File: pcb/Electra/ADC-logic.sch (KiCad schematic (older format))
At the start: 6 parts, among them J701 Conn_01x02_Female, J702 Conn_01x02_Female

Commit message: PCB Ver 1 completed (TODO: Check)
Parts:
- J701, J702: Package Reference - -> 2.54mm 1x2
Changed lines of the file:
@@
 $Descr A4 11693 8268
 encoding utf-8
-Sheet 7 7
+Sheet 7 8
 Title "Electra Project"
 Date "2021-03-21"
@@
 F 1 "1K" V 6250 4000 50  0000 L CNN
 F 2 "Resistor_SMD:R_0603_1608Metric_Pad0.98x0.95mm_HandSolder" V 6180 4050 50  0001 C CNN
-F 3 "~https://datasheet.lcsc.com/szlcsc/1811141223_UNI-ROYAL-Uniroyal-Elec-0603WAF1001T5E_C21190.pdf" H 6250 4050 50  0001 C CNN
+F 3 "https://datasheet.lcsc.com/szlcsc/1811141223_UNI-ROYAL-Uniroyal-Elec-0603WAF1001T5E_C21190.pdf" H 6250 4050 50  0001 C CNN
 F 4 "1kΩ ±1% 0.1W ±100ppm/℃ 0603 Chip Resistor - Surface Mount RoHS" H 6250 4050 50  0001 C CNN "Description"
 F 5 "C21190" H 6250 4050 50  0001 C CNN "LCSC Part #"
@@
 F 7 "-" H 5750 3000 50  0001 C CNN "Maximum Value"
 F 8 "-" H 5750 3000 50  0001 C CNN "Mfr.Part #"
-F 9 "-" H 5750 3000 50  0001 C CNN "Package Reference"
+F 9 "2.54mm 1x2" H 5750 3000 50  0001 C CNN "Package Reference"
 	1    5750 3000
 	0    -1   -1   0
@@
 F 7 "-" H 5750 3450 50  0001 C CNN "Maximum Value"
 F 8 "-" H 5750 3450 50  0001 C CNN "Mfr.Part #"
-F 9 "-" H 5750 3450 50  0001 C CNN "Package Reference"
+F 9 "2.54mm 1x2" H 5750 3450 50  0001 C CNN "Package Reference"
 	1    5750 3450
 	0    -1   -1   0
@@
 F 1 "ADC" H 6900 3700 50  0000 L CNN
 F 2 "TestPoint:TestPoint_Pad_D1.5mm" H 7050 3650 50  0001 C CNN
-F 3 "~" H 7050 3650 50  0001 C CNN
+F 3 "-" H 7050 3650 50  0001 C CNN
 F 4 "-" H 6850 3650 50  0001 C CNN "Description"
 F 5 "-" H 6850 3650 50  0001 C CNN "LCSC Part #"

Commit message: PCB completed (added silkscreen more)
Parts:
- J701: value Conn_01x02_Female -> A
- J702: value Conn_01x02_Female -> A2
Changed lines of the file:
@@
 AR Path="/60D35C7F" Ref="J?"  Part="1"
 AR Path="/60D319D8/60D35C7F" Ref="J701"  Part="1"
-F 0 "J701" V 5800 2950 50  0000 L CNN
-F 1 "Conn_01x02_Female" H 5800 3000 50  0001 L CNN
+F 0 "J701" V 5500 2850 50  0000 L CNN
+F 1 "A" V 5600 2800 50  0000 L CNN
 F 2 "Connector_JST:JST_XH_B2B-XH-A_1x02_P2.50mm_Vertical" H 5750 3000 50  0001 C CNN
 F 3 "-" H 5750 3000 50  0001 C CNN
@@
 AR Path="/60D35C9C" Ref="J?"  Part="1"
 AR Path="/60D319D8/60D35C9C" Ref="J702"  Part="1"
-F 0 "J702" V 5800 3400 50  0000 L CNN
-F 1 "Conn_01x02_Female" H 5800 3450 50  0001 L CNN
+F 0 "J702" V 5500 3300 50  0000 L CNN
+F 1 "A2" V 5600 3200 50  0000 L CNN
 F 2 "Connector_JST:JST_XH_B2B-XH-A_1x02_P2.50mm_Vertical" H 5750 3450 50  0001 C CNN
 F 3 "-" H 5750 3450 50  0001 C CNN

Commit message: Rev 2 completed, todo check all and remove not needed filed
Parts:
- J601: renamed from J701; Description - -> (none); LCSC Part # - -> (none); Manufacturer - -> (none); Maximum Value - -> (none); Mfr.Part # - -> (none)
- J602: renamed from J702; Description - -> (none); LCSC Part # - -> (none); Manufacturer - -> (none); Maximum Value - -> (none); Mfr.Part # - -> (none)
- R601: renamed from R701; value 3.57K -> 3.3K; Description 3.57kΩ ±1% 0.1W ±100ppm/℃ 0603 Chip Resistor - Surface Moun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 -> (none); LCSC (none) -> C22978; LCSC Part # C22998 -> (none); Manufacturer UNI-ROYAL(Uniroyal Elec) -> (none); Mfr.Part # 0603WAF3571T5E -> (none)
- R602: renamed from R702; Description 7.5kΩ ±1% 0.1W ±100ppm/℃ 0603 Chip Resistor - Surface Mount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 -> (none); LCSC (none) -> C23234; LCSC Part # C23234 -> (none); Manufacturer UNI-ROYAL(Uniroyal Elec) -> (none); Mfr.Part # 0603WAF7501T5E -> (none)
- R603: renamed from R703; Description 1kΩ ±1% 0.1W ±100ppm/℃ 0603 Chip Resistor - Surface Mount R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 -> (none); LCSC (none) -> C21190; LCSC Part # C21190 -> (none); Manufacturer UNI-ROYAL(Uniroyal Elec) -> (none); Mfr.Part # 0603WAF1001T5E -> (none)
- TP601: renamed from TP701; Description - -> (none); LCSC Part # - -> (none); Manufacturer - -> (none); Mfr.Part # - -> (none)
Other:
- note added: "Based on that, for R3 = 1K, R1 = 7.5R3 and R2=3.3R3\nVo1 ~~= 0.388V\nVo2 ~~= 0.767V\nVo ~~= 1.003V"
- note removed: "Based on that, for R3 = 1K, R1 = 7.5R3 and R2=3.5R3\nVo1 ~~= 0.39V\nVo2 ~~= 0.73V\nVo ~~= 0.97V"
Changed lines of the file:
@@
 $Descr A4 11693 8268
 encoding utf-8
-Sheet 7 8
+Sheet 6 8
 Title "Electra Project"
-Date "2021-03-21"
-Rev "1"
+Date "2021-04-01"
+Rev "2.0"
 Comp "Grehasopt"
 Comment1 "https://github.com/Grehasopt/Electra"
@@
 P 4700 3050
 AR Path="/60D35C67" Ref="#PWR?"  Part="1"
-AR Path="/60D319D8/60D35C67" Ref="#PWR0701"  Part="1"
-F 0 "#PWR0701" H 4700 2900 50  0001 C CNN
+AR Path="/60D319D8/60D35C67" Ref="#PWR0601"  Part="1"
+F 0 "#PWR0601" H 4700 2900 50  0001 C CNN
 F 1 "+3V3" H 4715 3223 50  0000 C CNN
 F 2 "" H 4700 3050 50  0001 C CNN
@@
 P 6250 4050
 AR Path="/60D35C6D" Ref="R?"  Part="1"
-AR Path="/60D319D8/60D35C6D" Ref="R703"  Part="1"
-F 0 "R703" H 6320 4096 50  0000 L CNN
+AR Path="/60D319D8/60D35C6D" Ref="R603"  Part="1"
+F 0 "R603" H 6320 4096 50  0000 L CNN
 F 1 "1K" V 6250 4000 50  0000 L CNN
 F 2 "Resistor_SMD:R_0603_1608Metric_Pad0.98x0.95mm_HandSolder" V 6180 4050 50  0001 C CNN
-F 3 "https://datasheet.lcsc.com/szlcsc/1811141223_UNI-ROYAL-Uniroyal-Elec-0603WAF1001T5E_C21190.pdf" H 6250 4050 50  0001 C CNN
-F 4 "1kΩ ±1% 0.1W ±100ppm/℃ 0603 Chip Resistor - Surface Mount RoHS" H 6250 4050 50  0001 C CNN "Description"
-F 5 "C21190" H 6250 4050 50  0001 C CNN "LCSC Part #"
-F 6 "UNI-ROYAL(Uniroyal Elec)" H 6250 4050 50  0001 C CNN "Manufacturer"
-F 7 "0.1W" H 6250 4050 50  0001 C CNN "Maximum Value"
-F 8 "0603WAF1001T5E" H 6250 4050 50  0001 C CNN "Mfr.Part #"
-F 9 "0603" H 6250 4050 50  0001 C CNN "Package Reference"
+F 3 "~" H 6250 4050 50  0001 C CNN
+F 4 "C21190" H 6250 4050 50  0001 C CNN "LCSC"
+F 5 "0.1W" H 6250 4050 50  0001 C CNN "Maximum Value"
+F 6 "0603" H 6250 4050 50  0001 C CNN "Package Reference"
 	1    6250 4050
 	1    0    0    -1
@@
 P 5200 3650
 AR Path="/60D35C73" Ref="R?"  Part="1"
-AR Path="/60D319D8/60D35C73" Ref="R702"  Part="1"
-F 0 "R702" V 5100 3650 50  0000 C CNN
+AR Path="/60D319D8/60D35C73" Ref="R602"  Part="1"
+F 0 "R602" V 5100 3650 50  0000 C CNN
 F 1 "7.5K" V 5200 3650 50  0000 C CNN
 F 2 "Resistor_SMD:R_0603_1608Metric_Pad0.98x0.95mm_HandSolder" V 5130 3650 50  0001 C CNN
-F 3 "https://datasheet.lcsc.com/szlcsc/1811081723_UNI-ROYAL-Uniroyal-Elec-0603WAF7501T5E_C23234.pdf" H 5200 3650 50  0001 C CNN
+F 3 "~" H 5200 3650 50  0001 C CNN
 F 4 "0603" H 5200 3650 50  0001 C CNN "Package Reference"
-F 5 "7.5kΩ ±1% 0.1W ±100ppm/℃ 0603 Chip Resistor - Surface Mount RoHS" H 5200 3650 50  0001 C CNN "Description"
-F 6 "C23234" H 5200 3650 50  0001 C CNN "LCSC Part #"
-F 7 "UNI-ROYAL(Uniroyal Elec)" H 5200 3650 50  0001 C CNN "Manufacturer"
-F 8 "0.1W" H 5200 3650 50  0001 C CNN "Maximum Value"
-F 9 "0603WAF7501T5E" H 5200 3650 50  0001 C CNN "Mfr.Part #"
+F 5 "C23234" H 5200 3650 50  0001 C CNN "LCSC"
+F 6 "0.1W" H 5200 3650 50  0001 C CNN "Maximum Value"
 	1    5200 3650
 	0    1    1    0
@@
 AR Path="/6086ADDC/60D35C7F" Ref="J?"  Part="1"
 AR Path="/60D35C7F" Ref="J?"  Part="1"
-AR Path="/60D319D8/60D35C7F" Ref="J701"  Part="1"
-F 0 "J701" V 5500 2850 50  0000 L CNN
+AR Path="/60D319D8/60D35C7F" Ref="J601"  Part="1"
+F 0 "J601" V 5500 2850 50  0000 L CNN
 F 1 "A" V 5600 2800 50  0000 L CNN
 F 2 "Connector_JST:JST_XH_B2B-XH-A_1x02_P2.50mm_Vertical" H 5750 3000 50  0001 C CNN
-F 3 "-" H 5750 3000 50  0001 C CNN
-F 4 "-" H 5750 3000 50  0001 C CNN "Description"
-F 5 "-" H 5750 3000 50  0001 C CNN "LCSC Part #"
-F 6 "-" H 5750 3000 50  0001 C CNN "Manufacturer"
-F 7 "-" H 5750 3000 50  0001 C CNN "Maximum Value"
-F 8 "-" H 5750 3000 50  0001 C CNN "Mfr.Part #"
-F 9 "2.54mm 1x2" H 5750 3000 50  0001 C CNN "Package Reference"
+F 3 "~" H 5750 3000 50  0001 C CNN
+F 4 "2.54mm 1x2" H 5750 3000 50  0001 C CNN "Package Reference"
 	1    5750 3000
 	0    -1   -1   0
@@
 P 6250 4300
 AR Path="/60D35C86" Ref="#PWR?"  Part="1"
-AR Path="/60D319D8/60D35C86" Ref="#PWR0702"  Part="1"
-F 0 "#PWR0702" H 6250 4050 50  0001 C CNN
+AR Path="/60D319D8/60D35C86" Ref="#PWR0602"  Part="1"
+F 0 "#PWR0602" H 6250 4050 50  0001 C CNN
 F 1 "GND" H 6150 4150 50  0000 C CNN
 F 2 "" H 6250 4300 50  0001 C CNN
@@
 AR Path="/6086ADDC/60D35C9C" Ref="J?"  Part="1"
 AR Path="/60D35C9C" Ref="J?"  Part="1"
-AR Path="/60D319D8/60D35C9C" Ref="J702"  Part="1"
-F 0 "J702" V 5500 3300 50  0000 L CNN
+AR Path="/60D319D8/60D35C9C" Ref="J602"  Part="1"
+F 0 "J602" V 5500 3300 50  0000 L CNN
 F 1 "A2" V 5600 3200 50  0000 L CNN
 F 2 "Connector_JST:JST_XH_B2B-XH-A_1x02_P2.50mm_Vertical" H 5750 3450 50  0001 C CNN
-F 3 "-" H 5750 3450 50  0001 C CNN
-F 4 "-" H 5750 3450 50  0001 C CNN "Description"
-F 5 "-" H 5750 3450 50  0001 C CNN "LCSC Part #"
-F 6 "-" H 5750 3450 50  0001 C CNN "Manufacturer"
-F 7 "-" H 5750 3450 50  0001 C CNN "Maximum Value"
-F 8 "-" H 5750 3450 50  0001 C CNN "Mfr.Part #"
-F 9 "2.54mm 1x2" H 5750 3450 50  0001 C CNN "Package Reference"
+F 3 "~" H 5750 3450 50  0001 C CNN
+F 4 "2.54mm 1x2" H 5750 3450 50  0001 C CNN "Package Reference"
 	1    5750 3450
 	0    -1   -1   0
@@
 P 6850 3650
 AR Path="/60D35CAE" Ref="TP?"  Part="1"
-AR Path="/60D319D8/60D35CAE" Ref="TP701"  Part="1"
-F 0 "TP701" H 6900 3800 50  0000 L CNN
+AR Path="/60D319D8/60D35CAE" Ref="TP601"  Part="1"
+F 0 "TP601" H 6900 3800 50  0000 L CNN
 F 1 "ADC" H 6900 3700 50  0000 L CNN
 F 2 "TestPoint:TestPoint_Pad_D1.5mm" H 7050 3650 50  0001 C CNN
-F 3 "-" H 7050 3650 50  0001 C CNN
-F 4 "-" H 6850 3650 50  0001 C CNN "Description"
-F 5 "-" H 6850 3650 50  0001 C CNN "LCSC Part #"
-F 6 "-" H 6850 3650 50  0001 C CNN "Manufacturer"
-F 7 "-" H 6850 3650 50  0001 C CNN "Maximum Value"
-F 8 "-" H 6850 3650 50  0001 C CNN "Mfr.Part #"
-F 9 "-" H 6850 3650 50  0001 C CNN "Package Reference"
+F 3 "~" H 7050 3650 50  0001 C CNN
+F 4 "-" H 6850 3650 50  0001 C CNN "Maximum Value"
+F 5 "-" H 6850 3650 50  0001 C CNN "Package Reference"
 	1    6850 3650
 	1    0    0    -1
@@
 P 5200 3200
 AR Path="/60D35C8C" Ref="R?"  Part="1"
-AR Path="/60D319D8/60D35C8C" Ref="R701"  Part="1"
-F 0 "R701" V 5100 3200 50  0000 C CNN
-F 1 "3.57K" V 5200 3200 50  0000 C CNN
+AR Path="/60D319D8/60D35C8C" Ref="R601"  Part="1"
+F 0 "R601" V 5100 3200 50  0000 C CNN
+F 1 "3.3K" V 5200 3200 50  0000 C CNN
 F 2 "Resistor_SMD:R_0603_1608Metric_Pad0.98x0.95mm_HandSolder" V 5130 3200 50  0001 C CNN
-F 3 "https://datasheet.lcsc.com/szlcsc/1811081715_UNI-ROYAL-Uniroyal-Elec-0603WAF3571T5E_C22998.pdf" H 5200 3200 50  0001 C CNN
+F 3 "~" H 5200 3200 50  0001 C CNN
 F 4 "0603" H 5200 3200 50  0001 C CNN "Package Reference"
-F 5 "3.57kΩ ±1% 0.1W ±100ppm/℃ 0603 Chip Resistor - Surface Mount RoHS" H 5200 3200 50  0001 C CNN "Description"
-F 6 "C22998" H 5200 3200 50  0001 C CNN "LCSC Part #"
-F 7 "UNI-ROYAL(Uniroyal Elec)" H 5200 3200 50  0001 C CNN "Manufacturer"
-F 8 "0.1W" H 5200 3200 50  0001 C CNN "Maximum Value"
-F 9 "0603WAF3571T5E" H 5200 3200 50  0001 C CNN "Mfr.Part #"
+F 5 "C22978" H 5200 3200 50  0001 C CNN "LCSC"
+F 6 "0.1W" H 5200 3200 50  0001 C CNN "Maximum Value"
 	1    5200 3200
 	0    1    1    0
 $EndComp
 Text Notes 1250 6950 0    79   ~ 0
-Based on that, for R3 = 1K, R1 = 7.5R3 and R2=3.5R3\nVo1 ~~=  0.39V\nVo2 ~~=  0.73V\nVo  ~~=  0.97V
+Based on that, for R3 = 1K, R1 = 7.5R3 and R2=3.3R3\nVo1 ~~=  0.388V\nVo2 ~~=  0.767V\nVo  ~~=  1.003V
 $EndSCHEMATC

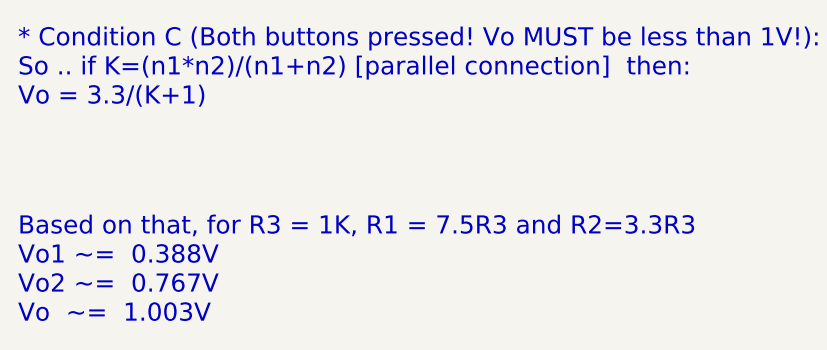
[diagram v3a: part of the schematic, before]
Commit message: Minor fixes on schematic and pcb fix bjt netlist + ac main voltage to both sides (Rev 2.1)
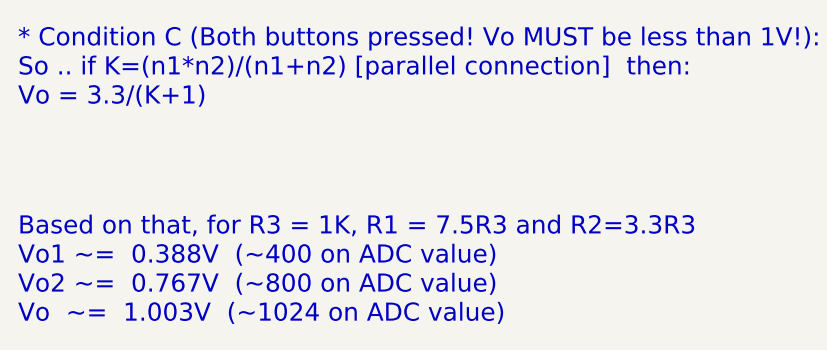
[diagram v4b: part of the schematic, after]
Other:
- note added: "Based on that, for R3 = 1K, R1 = 7.5R3 and R2=3.3R3\nVo1 ~~= 0.388V (~~400 on ADC value)\nVo2 ~~= 0.767V (~~800 on ADC value)\nVo ~~= 1.003V (~~1024 on ADC value)"
- note removed: "Based on that, for R3 = 1K, R1 = 7.5R3 and R2=3.3R3\nVo1 ~~= 0.388V\nVo2 ~~= 0.767V\nVo ~~= 1.003V"
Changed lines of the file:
@@
 Sheet 6 8
 Title "Electra Project"
-Date "2021-04-01"
-Rev "2.0"
+Date "2021-05-04"
+Rev "2.1"
 Comp "Grehasopt"
 Comment1 "https://github.com/Grehasopt/Electra"
@@
 $EndComp
 Text Notes 1250 6950 0    79   ~ 0
-Based on that, for R3 = 1K, R1 = 7.5R3 and R2=3.3R3\nVo1 ~~=  0.388V\nVo2 ~~=  0.767V\nVo  ~~=  1.003V
+Based on that, for R3 = 1K, R1 = 7.5R3 and R2=3.3R3\nVo1 ~~=  0.388V  (~~400 on ADC value)\nVo2 ~~=  0.767V  (~~800 on ADC value)\nVo  ~~=  1.003V  (~~1024 on ADC value)
 $EndSCHEMATC
